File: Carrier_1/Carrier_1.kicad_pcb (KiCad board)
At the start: 2 copper layers, 17 x 22.5 mm, 9 parts, among them J1 CH1, J2 HV, J3 CH2, J4 GND, U1 LGAD_2_pad

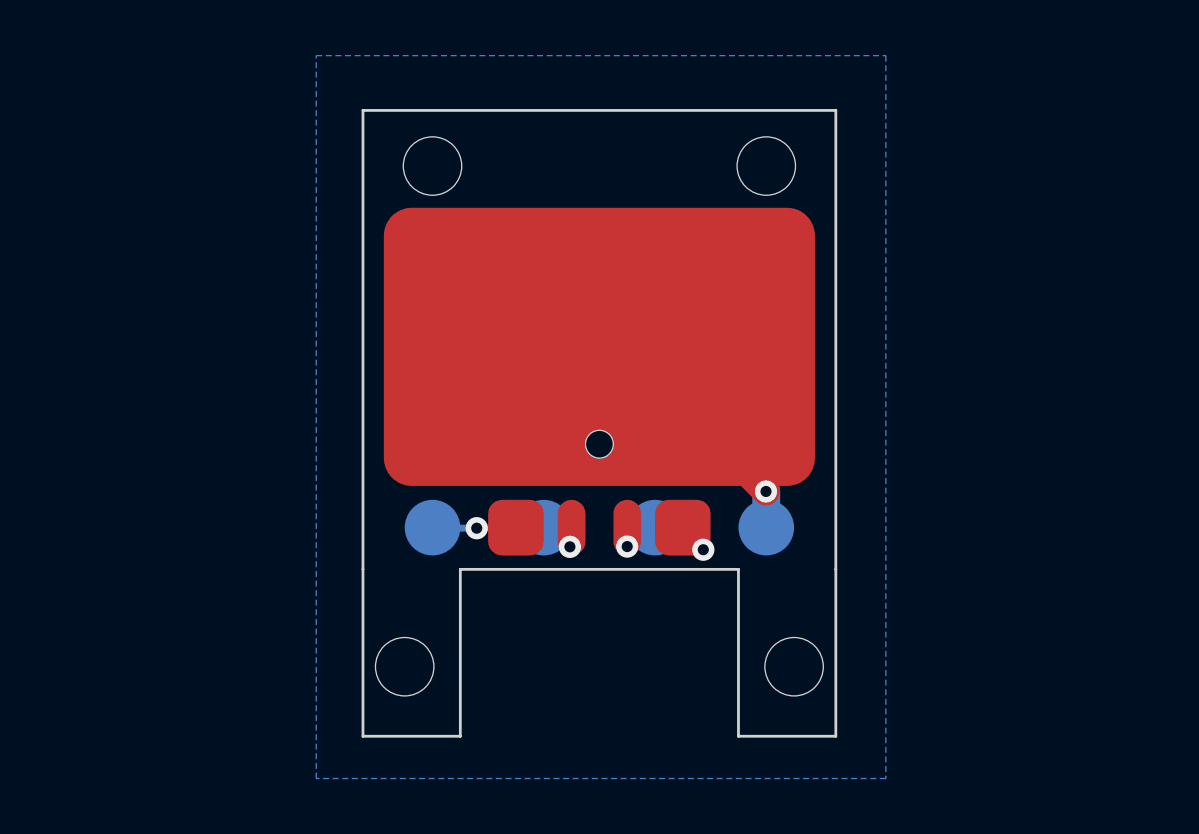
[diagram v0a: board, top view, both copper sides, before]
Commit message: Prototype with 4 channels
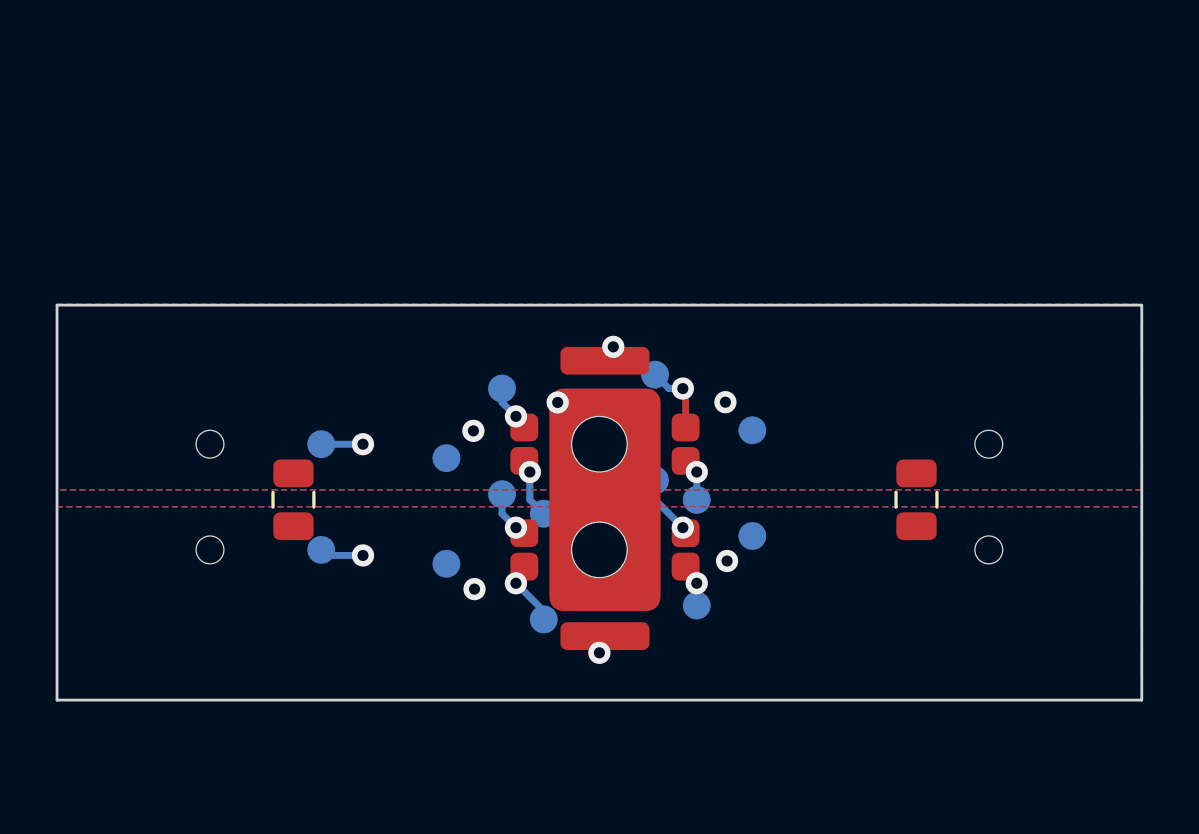
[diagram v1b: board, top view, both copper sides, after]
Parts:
- added C1: 100n, Capacitor_SMD:C_0805_2012Metric, F.Cu at (-11.0, 2.00)
- added C2: 100n, Capacitor_SMD:C_0805_2012Metric, F.Cu at (11.4, 2.00)
- added J10: CH1, chubut:MILL-MAX_0965-0-15-20-80-14-11-0_contact, B.Cu at (3.50, 2.00)
- added J11: CH1, chubut:MILL-MAX_0965-0-15-20-80-14-11-0_contact, B.Cu at (-2.00, 2.50)
- added J12: CH1, chubut:MILL-MAX_0965-0-15-20-80-14-11-0_contact, B.Cu at (-3.50, -2.00)
- added J13: CH1, chubut:MILL-MAX_0965-0-15-20-80-14-11-0_contact, B.Cu at (-5.50, 0.50)
- added J14: CH1, chubut:MILL-MAX_0965-0-15-20-80-14-11-0_contact, B.Cu at (5.50, -0.50)
- added J5: CH1, chubut:MILL-MAX_0965-0-15-20-80-14-11-0_contact, B.Cu at (5.50, 3.30)
- added J6: HV, chubut:MILL-MAX_0965-0-15-20-80-14-11-0_contact, B.Cu at (-10.0, 0.00)
- added J7: CH1, chubut:MILL-MAX_0965-0-15-20-80-14-11-0_contact, B.Cu at (2.00, -2.50)
- added J8: CH1, chubut:MILL-MAX_0965-0-15-20-80-14-11-0_contact, B.Cu at (-5.50, 4.30)
- added J9: HV, chubut:MILL-MAX_0965-0-15-20-80-14-11-0_contact, B.Cu at (-10.0, 3.80)
- H1, H2, H3, H4: footprint MountingHole:MountingHole_2.1mm -> chubut:MILL-MAX_0965-0-15-20-80-14-11-0_alignment_hole
- J2: value HV -> CH1
- J3: value CH2 -> CH1
- J4: value GND -> CH1
- U1: value LGAD_2_pad -> LGAD_4CH_dual; footprint chubut:LGAD -> chubut:LGAD_4CH_dual
- moved H1 22.4 mm to (14.0, 0.00)
- moved H2 22.4 mm to (-14.0, 0.00)
- moved H3 21.4 mm to (-14.0, 3.80)
- moved H4 21.4 mm to (14.0, 3.80)
- moved J3 5.19 mm to (-2.00, 6.30)
- moved J1 4.35 mm to (2.00, 1.30)
- moved J2 3.75 mm to (3.50, 5.80)
- moved J4 2.77 mm to (-3.50, 1.80)
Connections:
- J2 pad 1: /HV -> Net-(J2-Pad1)
- J4 pad 1: GND -> Net-(J4-Pad1)
- U1 pad 2: GND -> /GND2
- U1 pad 3: Net-(J3-Pad1) -> Net-(J12-Pad1)
- U1 pad 4: Net-(J1-Pad1) -> Net-(J11-Pad1)
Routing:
- net /HV: track 9.45 -> 3.08 mm, vias 1 -> 3
- net GND: track 4.11 -> 0.00 mm, vias 2 -> 0
- net Net-(J7-Pad1): track 0.00 -> 2.65 mm, vias 0 -> 1
- net Net-(J11-Pad1): track 0.00 -> 2.19 mm, vias 0 -> 1
- net Net-(J4-Pad1): track 0.00 -> 1.79 mm, vias 0 -> 1
- net Net-(J12-Pad1): track 0.00 -> 1.73 mm, vias 0 -> 1
- net Net-(J10-Pad1): track 0.00 -> 1.57 mm, vias 0 -> 1
- net Net-(J2-Pad1): track 0.00 -> 1.57 mm, vias 0 -> 1
- net /GND1: track 0.00 -> 0.68 mm, vias 0 -> 3
- net /GND2: track 0.00 -> 0.62 mm, vias 0 -> 3
- added copper zone on B.Cu, net /GND1
- added copper zone on F.Cu, net /GND1
- added copper zone on In1.Cu, net /GND1
- added copper zone on B.Cu, net /GND2
- added copper zone on F.Cu, net /GND2
- added copper zone on In1.Cu, net /GND2
- added copper zone on In2.Cu, net /HV
- removed copper zone on B.Cu, net GND
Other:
- board size 17 x 22.5 mm -> 39 x 14.2 mm
- copper layers 2 -> 4

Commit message: Fixed hardcoded path
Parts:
- U1: value LGAD_4CH_dual -> LGAD_4CH
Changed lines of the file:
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@@
       (effects (font (size 0.5 0.5) (thickness 0.08)))
     )
+    (fp_line (start -0.261252 0.735) (end 0.261252 0.735) (layer "F.SilkS") (width 0.12))
     (fp_line (start -0.261252 -0.735) (end 0.261252 -0.735) (layer "F.SilkS") (width 0.12))
-    (fp_line (start -0.261252 0.735) (end 0.261252 0.735) (layer "F.SilkS") (width 0.12))
+    (fp_line (start 1.7 -0.98) (end 1.7 0.98) (layer "F.CrtYd") (width 0.05))
     (fp_line (start -1.7 0.98) (end -1.7 -0.98) (layer "F.CrtYd") (width 0.05))
+    (fp_line (start 1.7 0.98) (end -1.7 0.98) (layer "F.CrtYd") (width 0.05))
     (fp_line (start -1.7 -0.98) (end 1.7 -0.98) (layer "F.CrtYd") (width 0.05))
-    (fp_line (start 1.7 -0.98) (end 1.7 0.98) (layer "F.CrtYd") (width 0.05))
-    (fp_line (start 1.7 0.98) (end -1.7 0.98) (layer "F.CrtYd") (width 0.05))
+    (fp_line (start -1 0.625) (end -1 -0.625) (layer "F.Fab") (width 0.1))
     (fp_line (start -1 -0.625) (end 1 -0.625) (layer "F.Fab") (width 0.1))
+    (fp_line (start 1 0.625) (end -1 0.625) (layer "F.Fab") (width 0.1))
     (fp_line (start 1 -0.625) (end 1 0.625) (layer "F.Fab") (width 0.1))
-    (fp_line (start 1 0.625) (end -1 0.625) (layer "F.Fab") (width 0.1))
-    (fp_line (start -1 0.625) (end -1 -0.625) (layer "F.Fab") (width 0.1))
     (pad "1" smd roundrect (at -0.95 0 90) (size 1 1.45) (layers "F.Cu" "F.Paste" "F.Mask") (roundrect_rratio 0.25)
       (net 10 "/GND1") (pintype "passive"))
@@
       (effects (font (size 1 1) (thickness 0.15)))
     )
-    (fp_text value "LGAD_4CH_dual" (at 0 8.62 unlocked) (layer "F.Fab")
+    (fp_text value "LGAD_4CH" (at 0 8.62 unlocked) (layer "F.Fab")
       (effects (font (size 1 1) (thickness 0.15)))
     )
@@
     (pad "11" smd roundrect (at 3.1 3.2) (size 1 1) (layers "F.Cu" "F.Mask") (roundrect_rratio 0.25)
       (net 3 "Net-(J1-Pad1)") (pintype "unspecified"))
-    (model "/home/alf/cernbox/projects/LGAD_stability/Chubut_2/libs/3D/LGAD_market_survey_FBK.step"
+    (model "${KIPRJMOD}/../libs/3D/LGAD_market_survey_FBK.step"
       (offset (xyz 0.2 -2 0))
       (scale (xyz 1 1 1))
@@
     (fp_line (start -0.261252 0.735) (end 0.261252 0.735) (layer "F.SilkS") (width 0.12))
     (fp_line (start -0.261252 -0.735) (end 0.261252 -0.735) (layer "F.SilkS") (width 0.12))
+    (fp_line (start 1.7 -0.98) (end 1.7 0.98) (layer "F.CrtYd") (width 0.05))
+    (fp_line (start -1.7 0.98) (end -1.7 -0.98) (layer "F.CrtYd") (width 0.05))
     (fp_line (start 1.7 0.98) (end -1.7 0.98) (layer "F.CrtYd") (width 0.05))
-    (fp_line (start -1.7 0.98) (end -1.7 -0.98) (layer "F.CrtYd") (width 0.05))
-    (fp_line (start 1.7 -0.98) (end 1.7 0.98) (layer "F.CrtYd") (width 0.05))
     (fp_line (start -1.7 -0.98) (end 1.7 -0.98) (layer "F.CrtYd") (width 0.05))
+    (fp_line (start -1 0.625) (end -1 -0.625) (layer "F.Fab") (width 0.1))
+    (fp_line (start -1 -0.625) (end 1 -0.625) (layer "F.Fab") (width 0.1))
     (fp_line (start 1 0.625) (end -1 0.625) (layer "F.Fab") (width 0.1))
-    (fp_line (start -1 -0.625) (end 1 -0.625) (layer "F.Fab") (width 0.1))
-    (fp_line (start -1 0.625) (end -1 -0.625) (layer "F.Fab") (width 0.1))
     (fp_line (start 1 -0.625) (end 1 0.625) (layer "F.Fab") (width 0.1))
     (pad "1" smd roundrect (at -0.95 0 90) (size 1 1.45) (layers "F.Cu" "F.Paste" "F.Mask") (roundrect_rratio 0.25)

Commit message: Updated carrier for new design
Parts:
- removed C1, C2: 100n, Capacitor_SMD:C_0805_2012Metric
- added H5: MountingHole, chubut:MILL-MAX_7625-0-00-15-00-00-03-0_alignment_hole, F.Cu at (12.0, 0.00)
- added H6: MountingHole, chubut:MILL-MAX_7625-0-00-15-00-00-03-0_alignment_hole, F.Cu at (12.0, 3.80)
- H1, H2, H3, H4: footprint chubut:MILL-MAX_0965-0-15-20-80-14-11-0_alignment_hole -> chubut:MILL-MAX_7625-0-00-15-00-00-03-0_alignment_hole
- U1: value LGAD_4CH -> LGAD_4CH_dual
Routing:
- net /HV: vias 3 -> 4
